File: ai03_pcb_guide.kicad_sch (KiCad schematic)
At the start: 16 parts

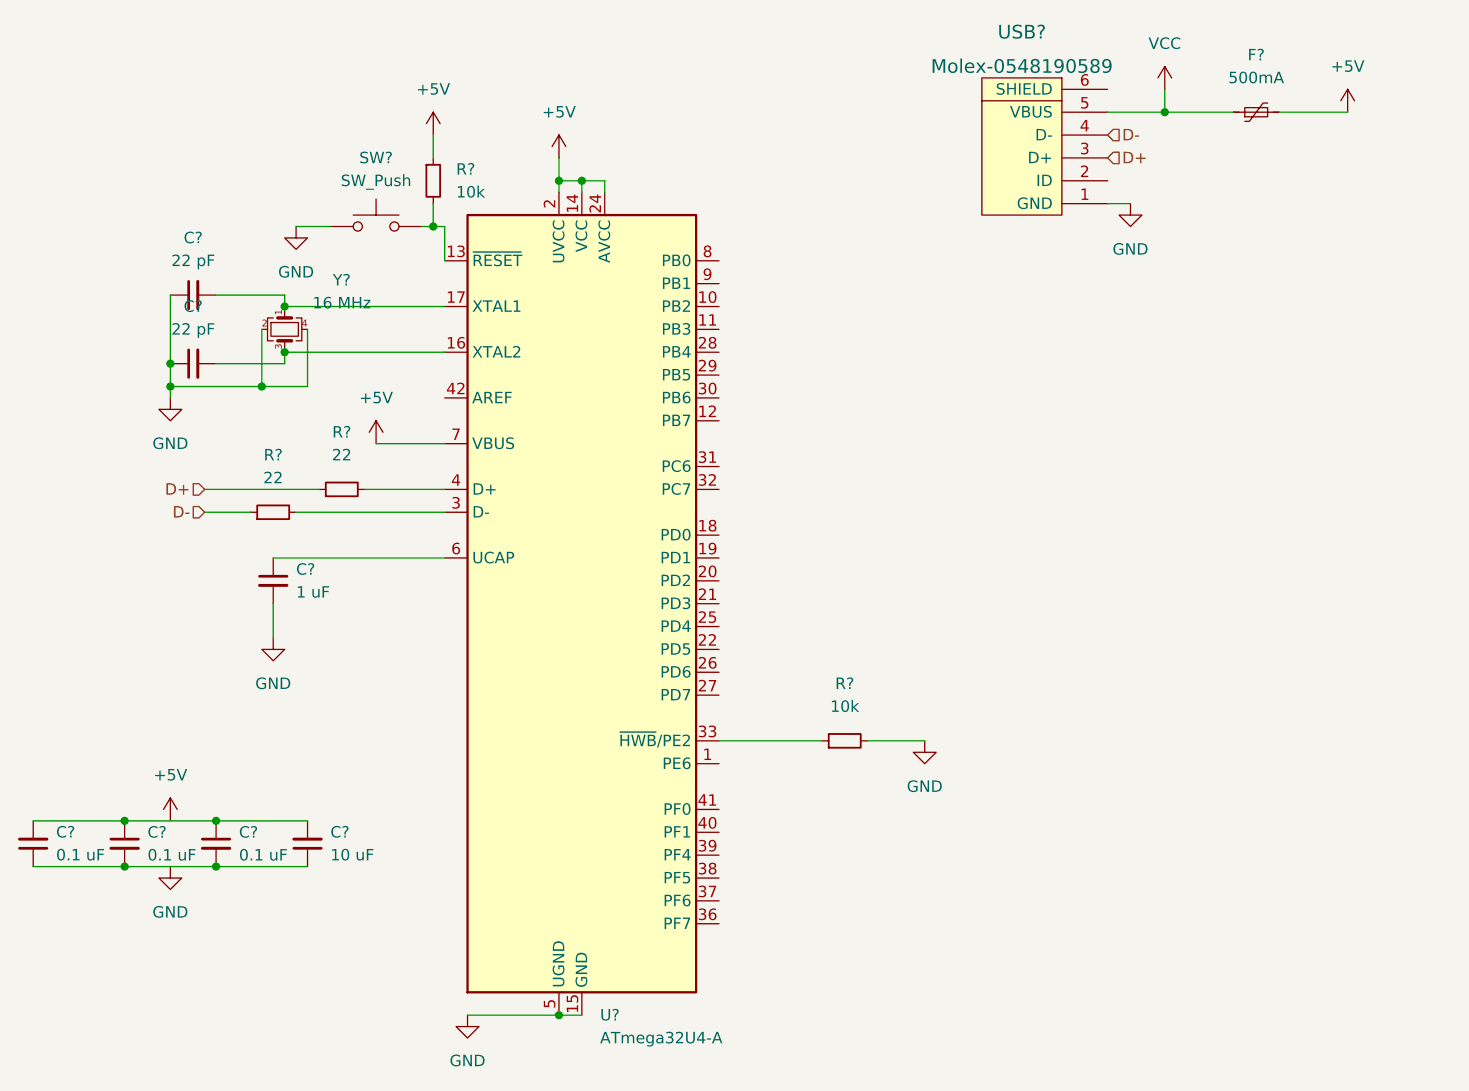
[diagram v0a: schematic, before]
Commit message: assign footprints to components in schematic
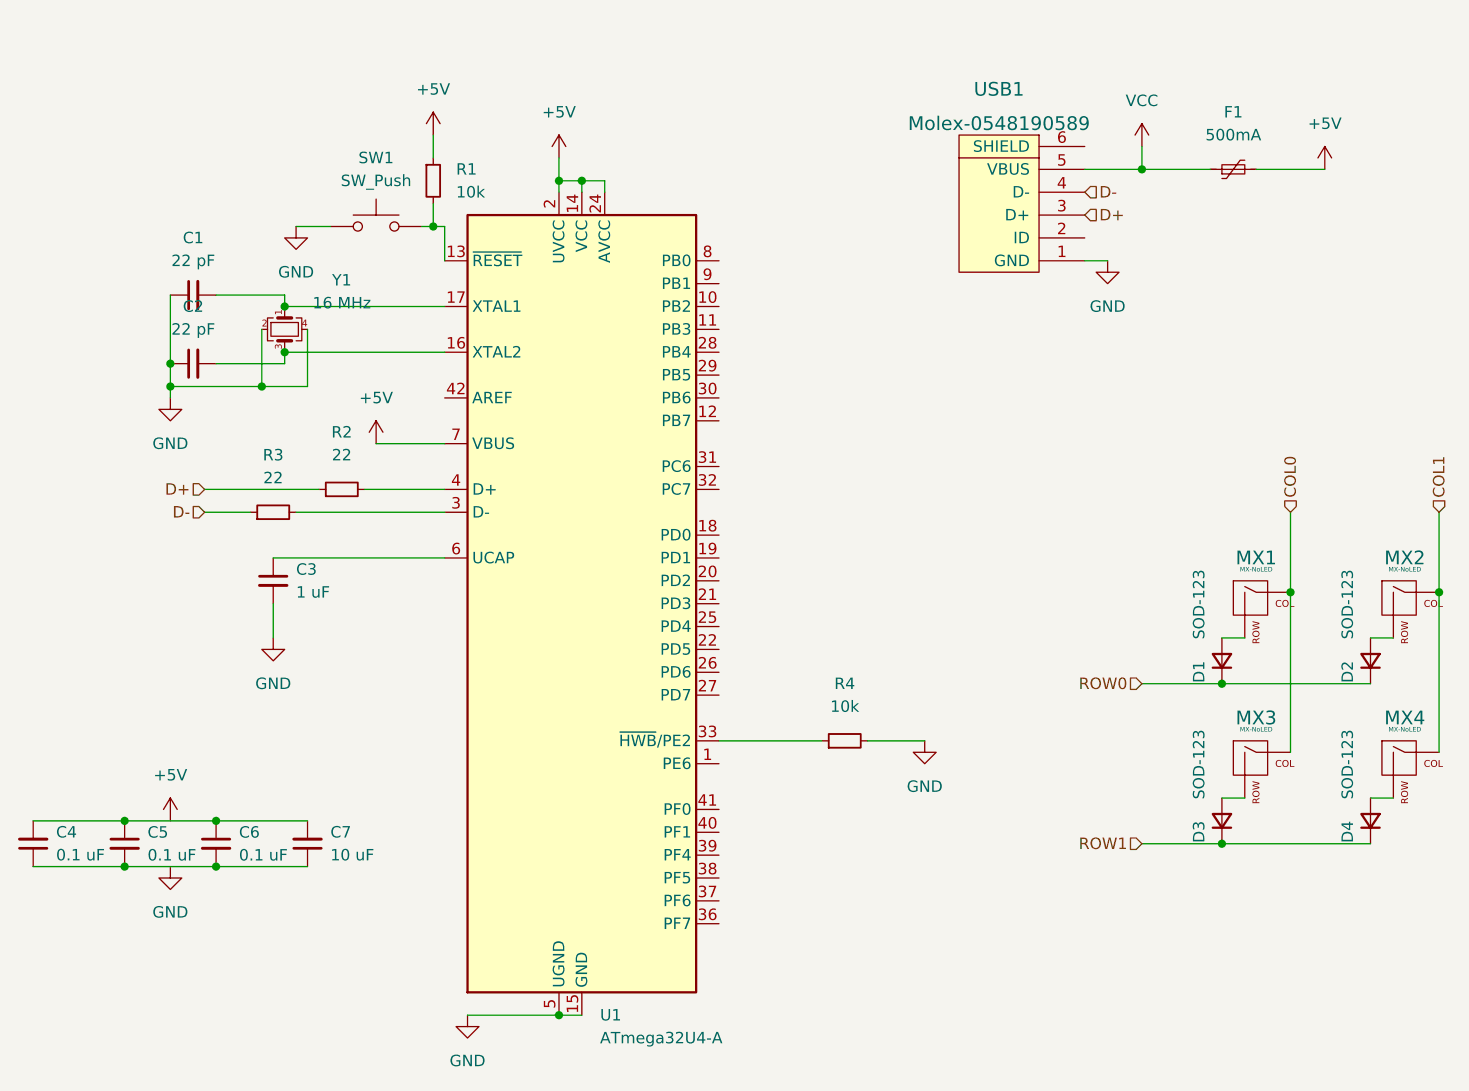
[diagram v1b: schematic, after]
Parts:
- added D1, D2, D3, D4: SOD-123, Diode_SMD:D_SOD-123, symbol Device:D_Small
- added MX1, MX2, MX3, MX4: MX-NoLED, MX_Alps_Hybrid:MX-1U-NoLED, symbol MX_Alps_Hybrid:MX-NoLED
- C1, C2, C3, C4, C5, C6, C7: renamed from C?; footprint (none) -> Capacitor_SMD:C_0805_2012Metric
- F1: renamed from F?; footprint (none) -> Fuse:Fuse_1206_3216Metric
- R1, R2, R3, R4: renamed from R?; footprint (none) -> Resistor_SMD:R_0805_2012Metric
- SW1: renamed from SW?; footprint (none) -> random-keyboard-parts:SKQG-1155865
- USB1: renamed from USB?; footprint (none) -> random-keyboard-parts:Molex-0548190589
- Y1: renamed from Y?; footprint (none) -> Crystal:Crystal_SMD_3225-4Pin_3.2x2.5mm
- gave numbers to parts that had none: 1
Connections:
- new net: D2.2 (A), MX2.2 (ROW)
- new net: D3.2 (A), MX3.2 (ROW)
- new net: D1.2 (A), MX1.2 (ROW)
- new net: D4.2 (A), MX4.2 (ROW)
- new net COL0: MX1.1 (COL), MX3.1 (COL)
- new net COL1: MX2.1 (COL), MX4.1 (COL)
- new net ROW0: D1.1 (K), D2.1 (K)
- new net ROW1: D3.1 (K), D4.1 (K)
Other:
- moved on the sheet: F1, USB1

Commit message: place components
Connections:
- net +5V: now also C4.2, C5.1, C6.1, C7.2
- net GND: now also C4.1, C5.2, C6.2, C7.1
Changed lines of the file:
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@@
   (junction (at 234.95 111.76) (diameter 0) (color 0 0 0 0)
+  )
+  (junction (at 93.98 142.24) (diameter 0) (color 0 0 0 0)
+  )
+  (junction (at 93.98 137.16) (diameter 0) (color 0 0 0 0)
   )
   (wire (pts (xy 201.93 64.77) (xy 209.55 64.77))
@@
     (stroke (width 0) (type default) (color 0 0 0 0))
   )
-  (wire (pts (xy 88.9 142.24) (xy 99.06 142.24))
+  (wire (pts (xy 88.9 142.24) (xy 93.98 142.24))
+    (stroke (width 0) (type default) (color 0 0 0 0))
+  )
+  (wire (pts (xy 93.98 137.16) (xy 99.06 137.16))
     (stroke (width 0) (type default) (color 0 0 0 0))
   )
@@
     (stroke (width 0) (type default) (color 0 0 0 0))
   )
-  (wire (pts (xy 88.9 137.16) (xy 99.06 137.16))
+  (wire (pts (xy 88.9 137.16) (xy 93.98 137.16))
     (stroke (width 0) (type default) (color 0 0 0 0))
   )
@@
     (stroke (width 0) (type default) (color 0 0 0 0))
   )
+  (wire (pts (xy 93.98 142.24) (xy 99.06 142.24))
+    (stroke (width 0) (type default) (color 0 0 0 0))
+  )

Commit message: routing
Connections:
- net COL0: now also U1.29 (PB5)
- net COL1: now also U1.28 (PB4)
- net ROW0: now also U1.27 (PD7)
- net ROW1: now also U1.30 (PB6)
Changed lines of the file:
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@@
+    (effects (font (size 1.27 1.27)) (justify left))
+  )
+  (hierarchical_label "ROW0" (shape input) (at 154.94 123.19 0)
     (effects (font (size 1.27 1.27)) (justify left))
   )
@@
     (effects (font (size 1.27 1.27)) (justify right))
   )
+  (hierarchical_label "ROW1" (shape input) (at 154.94 90.17 0)
+    (effects (font (size 1.27 1.27)) (justify left))
+  )
   (hierarchical_label "ROW0" (shape input) (at 201.93 121.92 180)
     (effects (font (size 1.27 1.27)) (justify right))
@@
     (effects (font (size 1.27 1.27)) (justify left))
   )
+  (hierarchical_label "COL0" (shape input) (at 154.94 87.63 0)
+    (effects (font (size 1.27 1.27)) (justify left))
+  )
+  (hierarchical_label "COL1" (shape input) (at 154.94 85.09 0)
+    (effects (font (size 1.27 1.27)) (justify left))
+  )
